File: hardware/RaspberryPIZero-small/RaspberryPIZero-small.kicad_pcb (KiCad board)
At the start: 2 copper layers, 68 x 51 mm, 29 parts, among them J1 RCVRY, J2 JTAG, J3 LPC, SW1 CPLD, SW2 BIOS

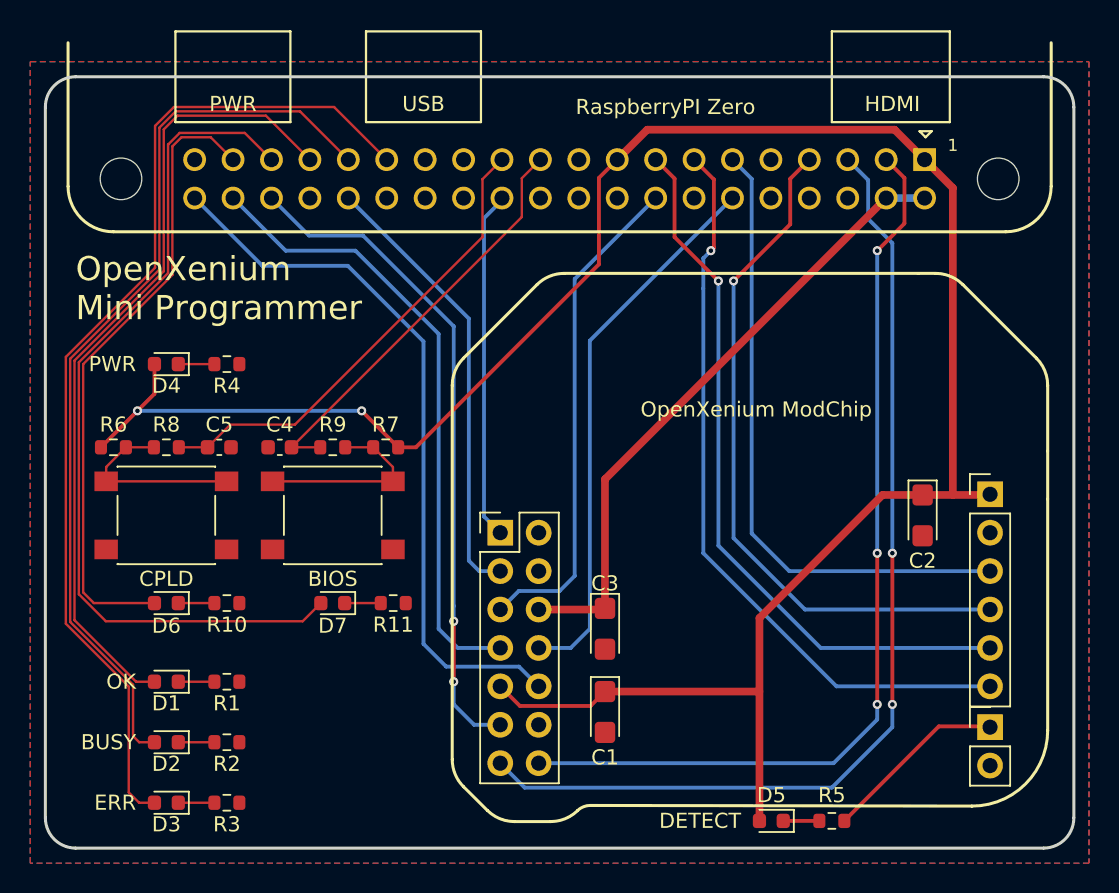
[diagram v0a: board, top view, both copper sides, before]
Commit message: added tooling holes to pcb & create JLCPCB manufacturing files
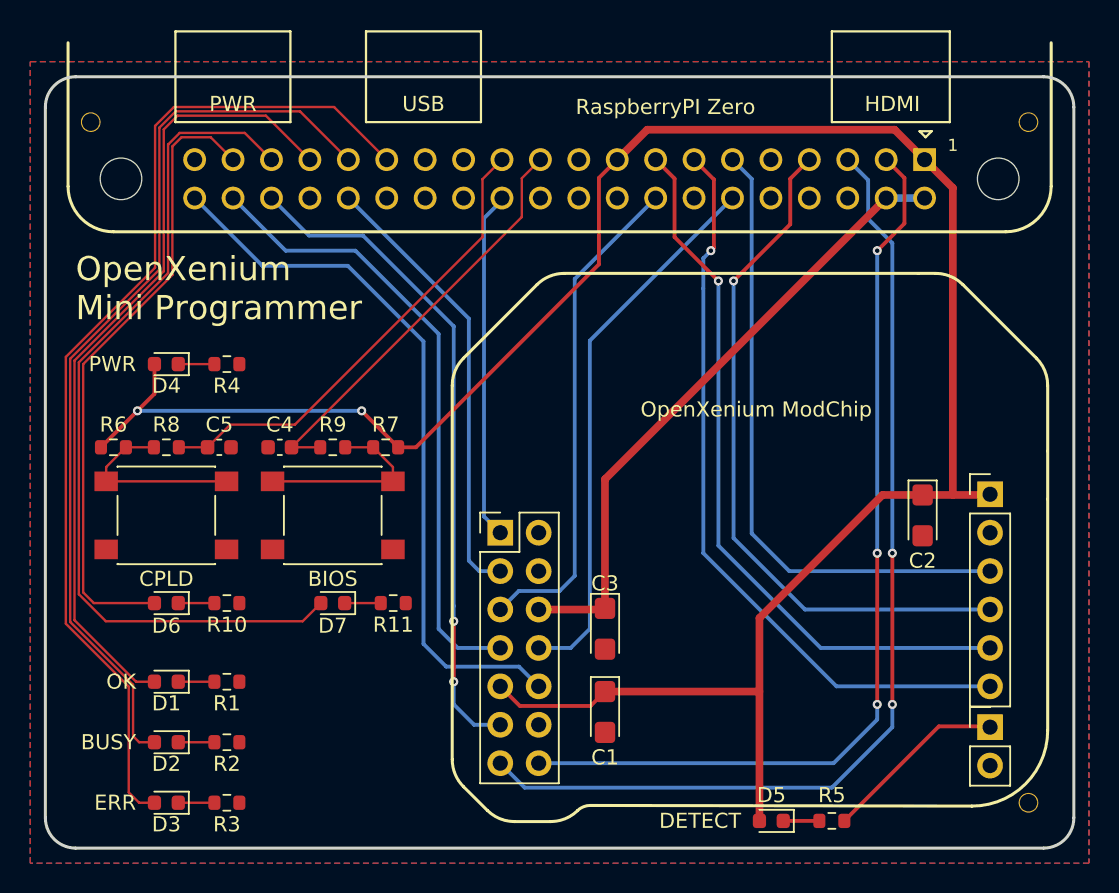
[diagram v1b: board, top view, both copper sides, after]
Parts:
- added REF**: JLCPCB_ToolingHole, 0-myparts:JLCPCB_ToolingHole, F.Cu at (50.0, 48.0)
- added REF**: JLCPCB_ToolingHole, 0-myparts:JLCPCB_ToolingHole, F.Cu at (112.0, 93.0)
- added REF**: JLCPCB_ToolingHole, 0-myparts:JLCPCB_ToolingHole, F.Cu at (112.0, 48.0)
- D6: value BUSY -> CPLD
- D7: value ERR -> BIOS
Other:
- board text added: "JLCJLCJLCJLC"

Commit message: modified board to support flashing 49LF002A
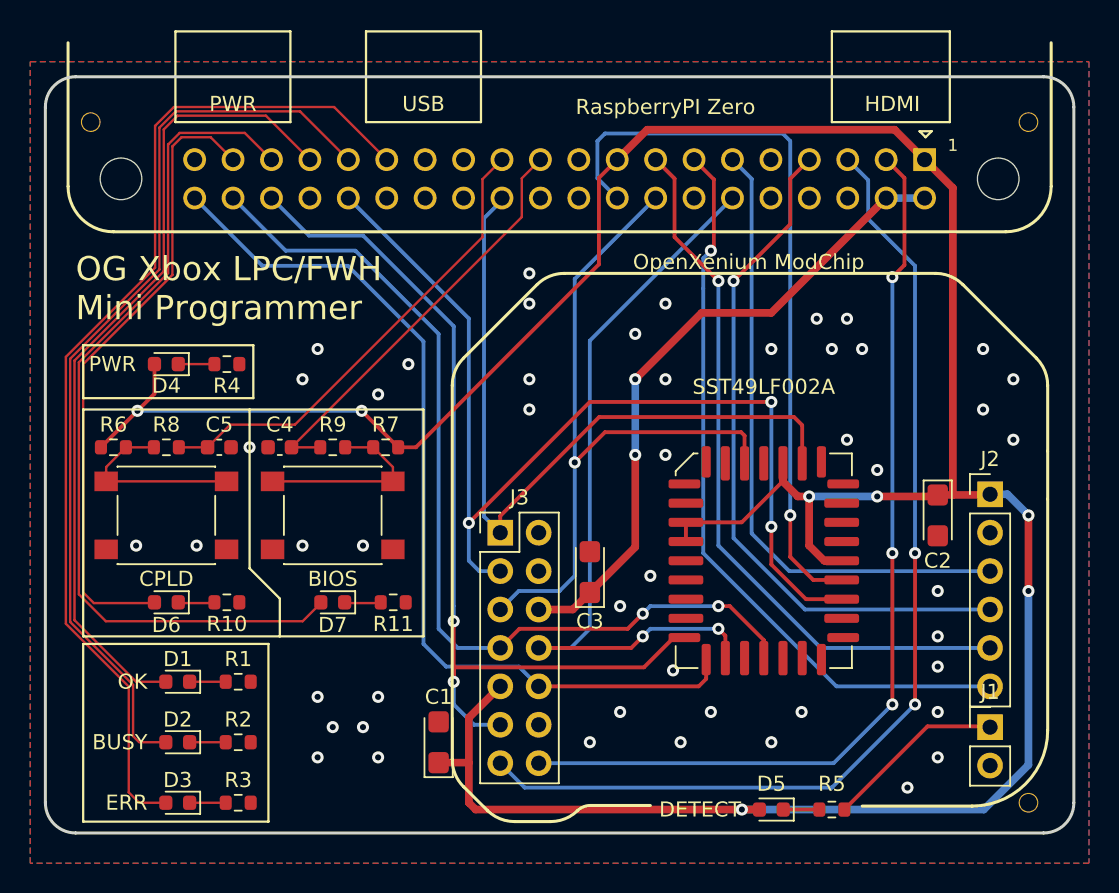
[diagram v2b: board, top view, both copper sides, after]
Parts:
- added U1: SST49LF002A, 0-myparts:PLCC-32-SOCKET-SMT, F.Cu at (94.5, 77.0)
- moved C1 11.2 mm to (73.0, 89.0), turned to 90 degrees
- moved C3 3.88 mm to (83.0, 77.8), turned to 90 degrees
- moved C2 1.00 mm to (106.0, 74.0)
- moved D1 0.75 mm to (55.8, 85.0)
- moved D2 0.75 mm to (55.8, 89.0)
- moved D3 0.75 mm to (55.8, 93.0)
- moved D5 0.75 mm to (95.0, 93.5)
- moved R1 0.75 mm to (59.8, 85.0)
- moved R2 0.75 mm to (59.8, 89.0)
- moved R3 0.75 mm to (59.8, 93.0)
- moved R5 0.75 mm to (99.0, 93.5)
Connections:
- RPI_ZERO1 pad 18: unconnected-(RPI_ZERO1-Pad18) -> /~{INIT}
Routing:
- net +3V3: track 146.0 -> 197.0 mm, vias 2 -> 7
- net /~{INIT}: track 0.00 -> 49.0 mm, vias 0 -> 1
- net /LFRAME: track 29.6 -> 69.3 mm, vias 0 -> 3
- net /LCLK: track 23.1 -> 49.6 mm
- net /LAD3: track 41.4 -> 62.1 mm, vias 0 -> 2
- net /LAD0: track 44.2 -> 61.2 mm
- net /LAD2: track 36.3 -> 50.8 mm, vias 0 -> 2
- net /LPC_RST: track 33.0 -> 47.0 mm, vias 0 -> 1
- net /LAD1: track 47.8 -> 60.4 mm
- net +5V: track 41.8 -> 43.3 mm, vias 0 -> 2
- net /SCL: track 67.0 -> 68.2 mm
- net /LED_OK: track 53.1 -> 53.9 mm
- net /LED_ERR: track 67.5 -> 68.2 mm
- net /LED_BUSY: track 60.2 -> 60.9 mm
- net GND: vias 0 -> 49
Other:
- board size 68 x 51 mm -> 68 x 50 mm
- board text added: "OG Xbox LPC/FWH Mini Programmer"
- board text removed: "OpenXenium Mini Programmer"
